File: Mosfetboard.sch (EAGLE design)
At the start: 26 parts, among them U1 3.3v

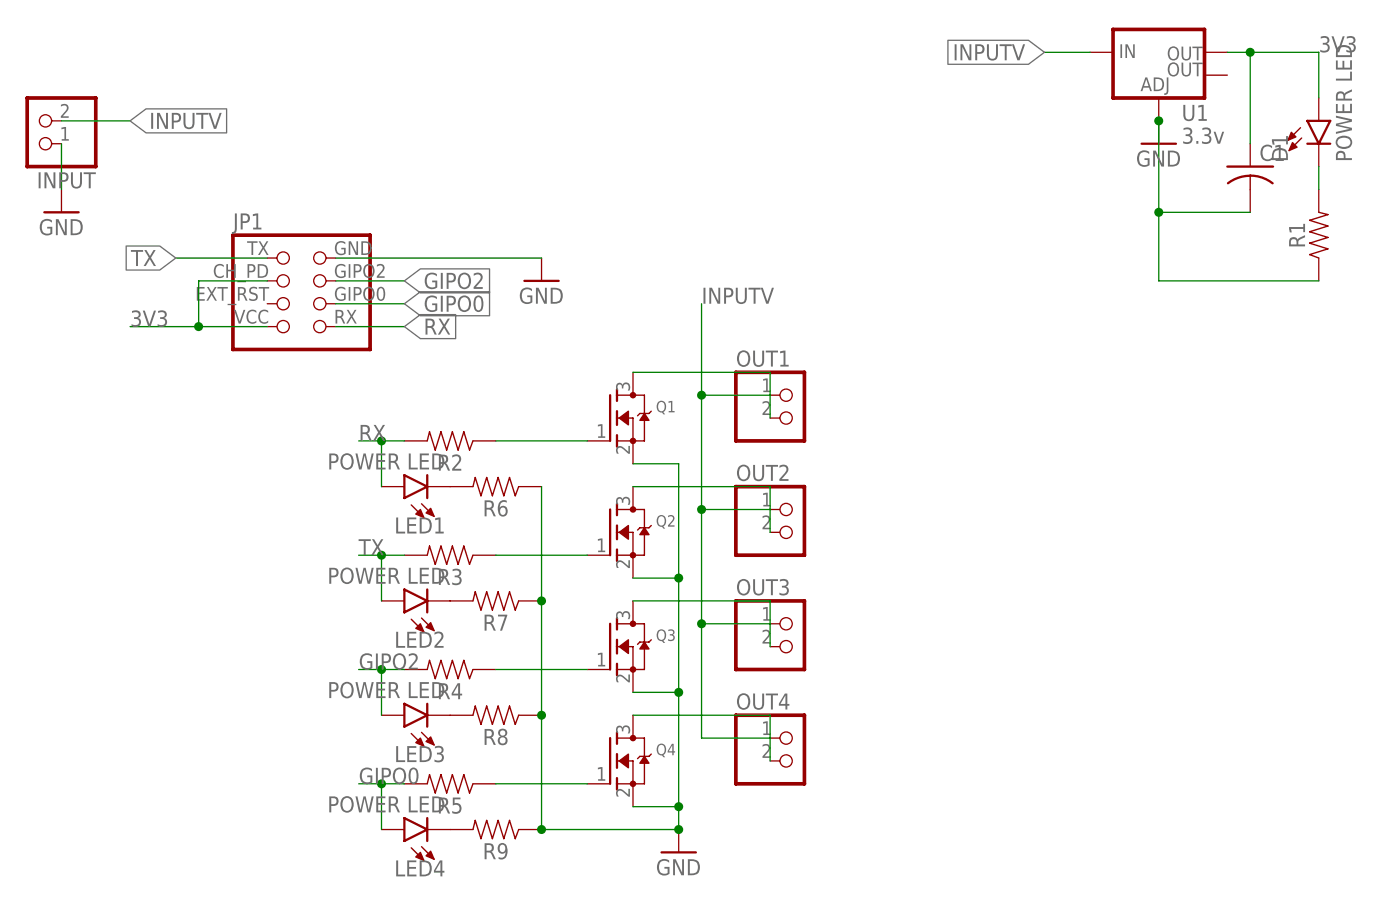
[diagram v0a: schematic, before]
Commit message: add values to resistors
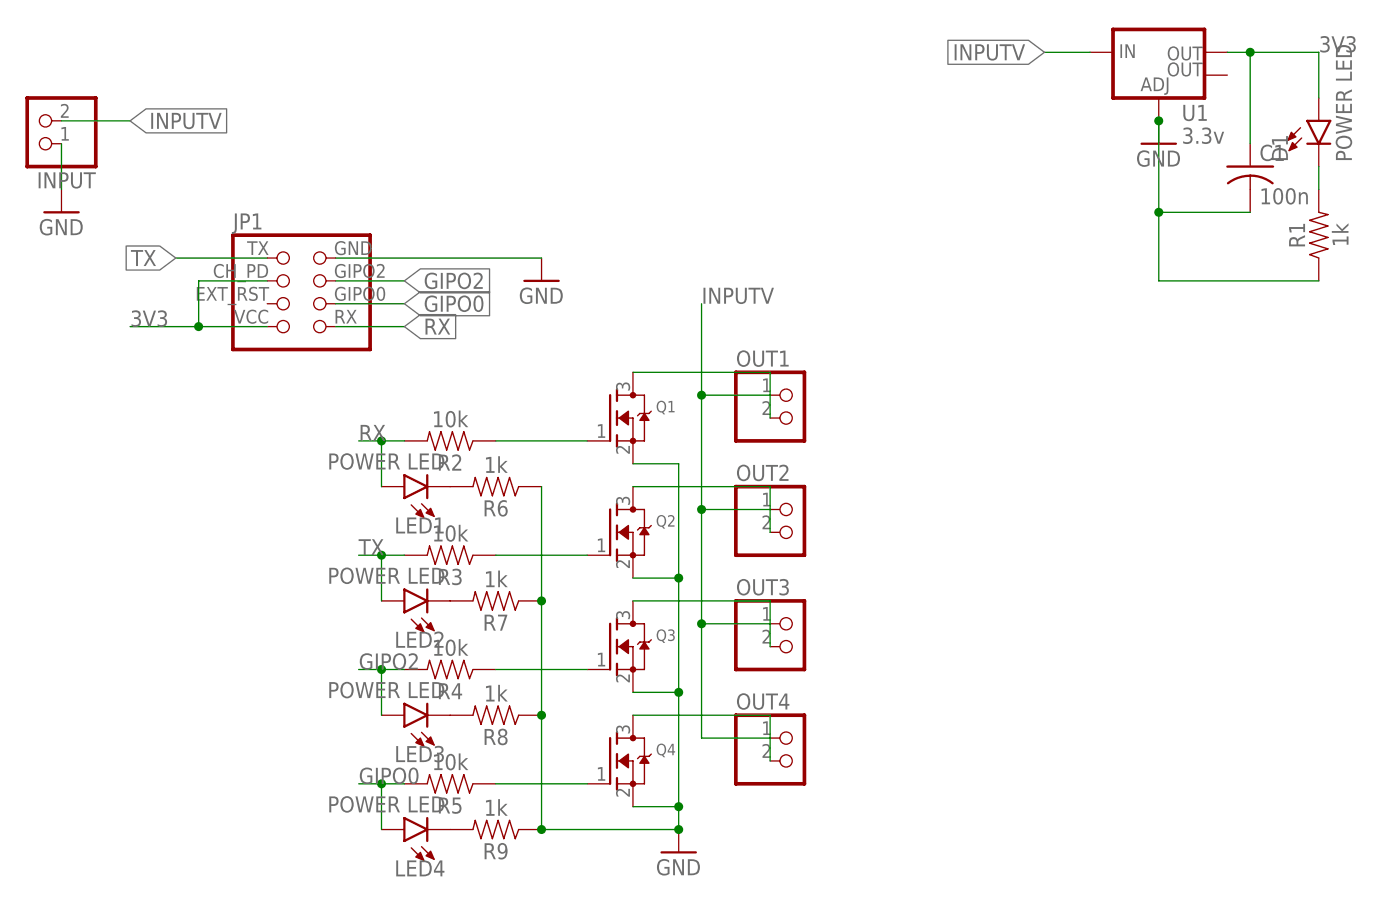
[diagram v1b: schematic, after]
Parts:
- C1: value (none) -> 100n
- R1, R6, R7, R8, R9: value (none) -> 1k
- R2, R3, R4, R5: value (none) -> 10k
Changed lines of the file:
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@@
 <part name="GND2" library="simple-shiled" library_urn="urn:adsk.eagle:library:80055" deviceset="GND" device=""/>
 <part name="D1" library="simple-shiled" library_urn="urn:adsk.eagle:library:80055" deviceset="LED-BLUE" device="0805" package3d_urn="urn:adsk.eagle:package:378040/2" value="POWER LED"/>
-<part name="R1" library="simple-shiled" library_urn="urn:adsk.eagle:library:80055" deviceset="RESISTOR" device="0805" package3d_urn="urn:adsk.eagle:package:103226/5" value=" "/>
-<part name="R2" library="simple-shiled" library_urn="urn:adsk.eagle:library:80055" deviceset="RESISTOR" device="0805" package3d_urn="urn:adsk.eagle:package:103226/5" value=" "/>
-<part name="R3" library="simple-shiled" library_urn="urn:adsk.eagle:library:80055" deviceset="RESISTOR" device="0805" package3d_urn="urn:adsk.eagle:package:103226/5" value=" "/>
-<part name="R4" library="simple-shiled" library_urn="urn:adsk.eagle:library:80055" deviceset="RESISTOR" device="0805" package3d_urn="urn:adsk.eagle:package:103226/5" value=" "/>
-<part name="R5" library="simple-shiled" library_urn="urn:adsk.eagle:library:80055" deviceset="RESISTOR" device="0805" package3d_urn="urn:adsk.eagle:package:103226/5" value=" "/>
-<part name="C1" library="simple-shiled" library_urn="urn:adsk.eagle:library:80055" deviceset="C-US" device="C1206K" package3d_urn="urn:adsk.eagle:package:878060/2"/>
+<part name="R1" library="simple-shiled" library_urn="urn:adsk.eagle:library:80055" deviceset="RESISTOR" device="0805" package3d_urn="urn:adsk.eagle:package:103226/5" value="1k"/>
+<part name="R2" library="simple-shiled" library_urn="urn:adsk.eagle:library:80055" deviceset="RESISTOR" device="0805" package3d_urn="urn:adsk.eagle:package:103226/5" value="10k"/>
+<part name="R3" library="simple-shiled" library_urn="urn:adsk.eagle:library:80055" deviceset="RESISTOR" device="0805" package3d_urn="urn:adsk.eagle:package:103226/5" value="10k"/>
+<part name="R4" library="simple-shiled" library_urn="urn:adsk.eagle:library:80055" deviceset="RESISTOR" device="0805" package3d_urn="urn:adsk.eagle:package:103226/5" value="10k"/>
+<part name="R5" library="simple-shiled" library_urn="urn:adsk.eagle:library:80055" deviceset="RESISTOR" device="0805" package3d_urn="urn:adsk.eagle:package:103226/5" value="10k"/>
+<part name="C1" library="simple-shiled" library_urn="urn:adsk.eagle:library:80055" deviceset="C-US" device="C1206K" package3d_urn="urn:adsk.eagle:package:878060/2" value="100n"/>
 <part name="LED1" library="simple-shiled" library_urn="urn:adsk.eagle:library:80055" deviceset="LED-BLUE" device="0805" package3d_urn="urn:adsk.eagle:package:378040/2" value="POWER LED"/>
 <part name="LED2" library="simple-shiled" library_urn="urn:adsk.eagle:library:80055" deviceset="LED-BLUE" device="0805" package3d_urn="urn:adsk.eagle:package:378040/2" value="POWER LED"/>
 <part name="LED3" library="simple-shiled" library_urn="urn:adsk.eagle:library:80055" deviceset="LED-BLUE" device="0805" package3d_urn="urn:adsk.eagle:package:378040/2" value="POWER LED"/>
 <part name="LED4" library="simple-shiled" library_urn="urn:adsk.eagle:library:80055" deviceset="LED-BLUE" device="0805" package3d_urn="urn:adsk.eagle:package:378040/2" value="POWER LED"/>
-<part name="R6" library="simple-shiled" library_urn="urn:adsk.eagle:library:80055" deviceset="RESISTOR" device="0805" package3d_urn="urn:adsk.eagle:package:103226/5" value=" "/>
-<part name="R7" library="simple-shiled" library_urn="urn:adsk.eagle:library:80055" deviceset="RESISTOR" device="0805" package3d_urn="urn:adsk.eagle:package:103226/5" value=" "/>
-<part name="R8" library="simple-shiled" library_urn="urn:adsk.eagle:library:80055" deviceset="RESISTOR" device="0805" package3d_urn="urn:adsk.eagle:package:103226/5" value=" "/>
-<part name="R9" library="simple-shiled" library_urn="urn:adsk.eagle:library:80055" deviceset="RESISTOR" device="0805" package3d_urn="urn:adsk.eagle:package:103226/5" value=" "/>
+<part name="R6" library="simple-shiled" library_urn="urn:adsk.eagle:library:80055" deviceset="RESISTOR" device="0805" package3d_urn="urn:adsk.eagle:package:103226/5" value="1k"/>
+<part name="R7" library="simple-shiled" library_urn="urn:adsk.eagle:library:80055" deviceset="RESISTOR" device="0805" package3d_urn="urn:adsk.eagle:package:103226/5" value="1k"/>
+<part name="R8" library="simple-shiled" library_urn="urn:adsk.eagle:library:80055" deviceset="RESISTOR" device="0805" package3d_urn="urn:adsk.eagle:package:103226/5" value="1k"/>
+<part name="R9" library="simple-shiled" library_urn="urn:adsk.eagle:library:80055" deviceset="RESISTOR" device="0805" package3d_urn="urn:adsk.eagle:package:103226/5" value="1k"/>
 </parts>
 <sheets>
